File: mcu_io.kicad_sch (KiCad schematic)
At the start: 10 parts, among them U3 SiWG917Y, U9 PCAL6408AHK

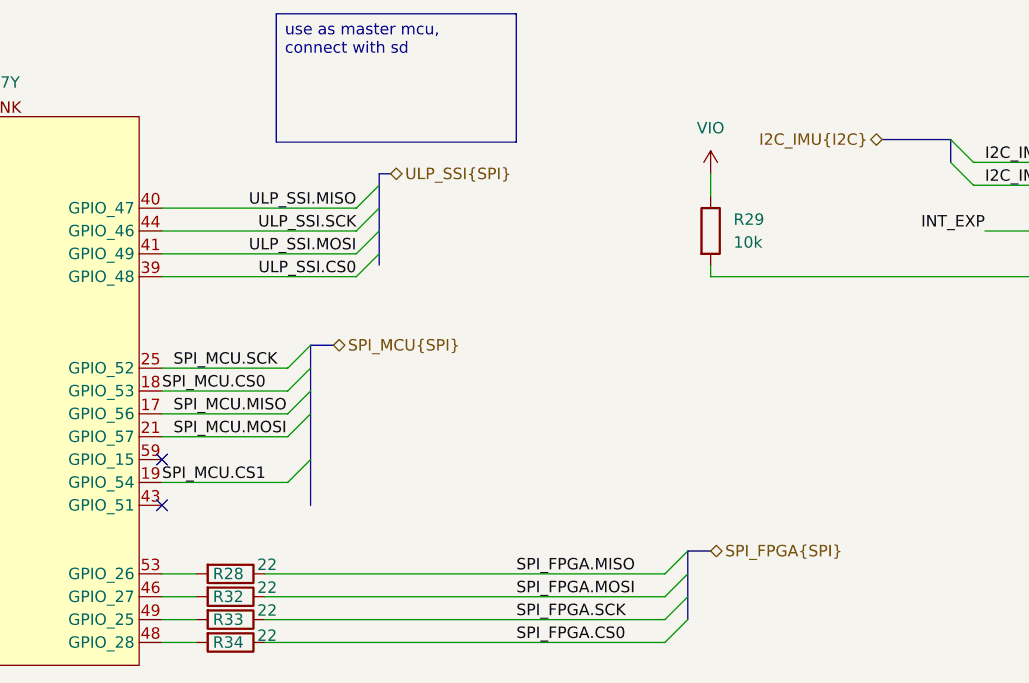
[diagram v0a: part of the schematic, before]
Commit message: new debug connector SOICbite, new board shape, new placement, addition of 22 ohm resistance in fast digital signals as spi
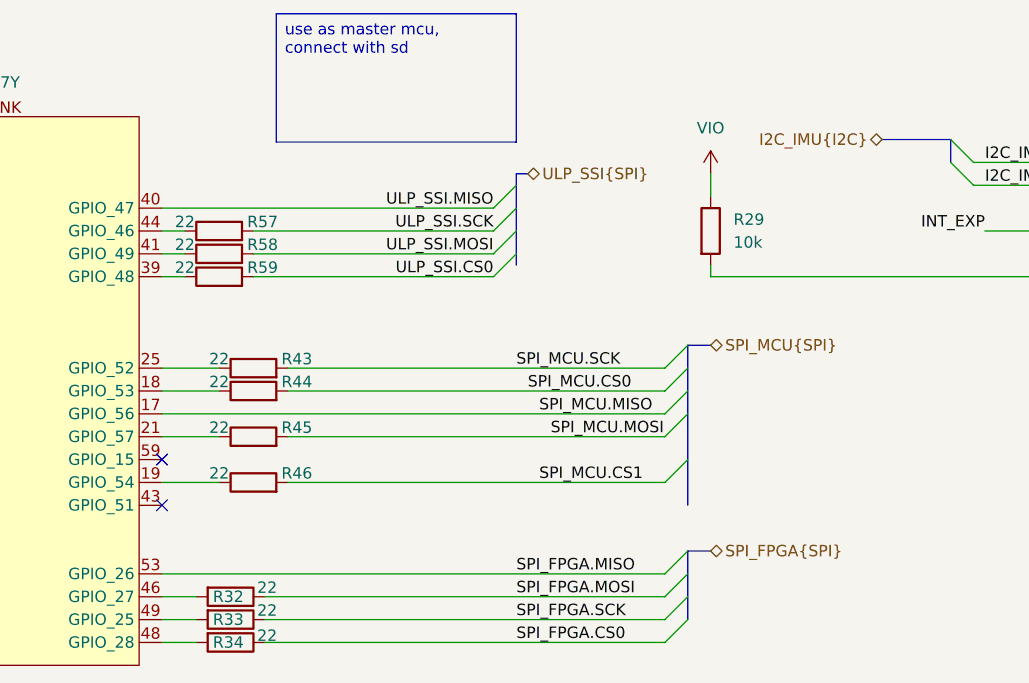
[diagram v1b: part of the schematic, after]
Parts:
- removed R28: 22, Resistor_SMD:R_0402_1005Metric, symbol #dzdb:g_res/R-22-0402
- added R43, R44, R45, R46, R57, R58, R59: 22, Resistor_SMD:R_0201_0603Metric, symbol #dzdb:g_res/R-22-0201
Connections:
- net SPI_FPGA.MISO: now also U3.53 (GPIO_26)
- net SPI_MCU.CS0: now also R44.2; no longer U3.18 (GPIO_53)
- net SPI_MCU.CS1: now also R46.2; no longer U3.19 (GPIO_54)
- net SPI_MCU.MOSI: now also R45.2; no longer U3.21 (GPIO_57)
- net SPI_MCU.SCK: now also R43.2; no longer U3.25 (GPIO_52)
- net ULP_SSI.CS0: now also R59.2; no longer U3.39 (GPIO_48)
- net ULP_SSI.MOSI: now also R58.2; no longer U3.41 (GPIO_49)
- net ULP_SSI.SCK: now also R57.2; no longer U3.44 (GPIO_46)
- new net: R43.1, U3.25 (GPIO_52)
- new net: R45.1, U3.21 (GPIO_57)
- new net: R46.1, U3.19 (GPIO_54)
- new net: R59.1, U3.39 (GPIO_48)
- new net: R44.1, U3.18 (GPIO_53)
- new net: R58.1, U3.41 (GPIO_49)
- new net: R57.1, U3.44 (GPIO_46)

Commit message: Comments on layout
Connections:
- net SPI_FPGA.CS0: now also R44.2; no longer R34.1
- net SPI_FPGA.MISO: now also U3.17 (GPIO_56); no longer U3.53 (GPIO_26)
- net SPI_FPGA.MOSI: now also R45.2; no longer R32.1
- net SPI_FPGA.SCK: now also R43.2; no longer R33.1
- net SPI_MCU.CS0: now also R34.1; no longer R44.2
- net SPI_MCU.MISO: now also U3.53 (GPIO_26); no longer U3.17 (GPIO_56)
- net SPI_MCU.MOSI: now also R32.1; no longer R45.2
- net SPI_MCU.SCK: now also R33.1; no longer R43.2
- net at R46.1: now also U3.47 (GPIO_29); no longer U3.19 (GPIO_54)
- no-connect marks 9 -> 8
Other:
- moved on the sheet: R46
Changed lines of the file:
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@@
-	)
-	(no_connect
-		(at 55.88 73.66)
 	)
 	(no_connect
@@
 	(wire
 		(pts
+			(xy 49.53 73.66) (xy 55.88 73.66)
+		)
+		(stroke
+			(width 0)
+			(type default)
+		)
+	)
+	(wire
+		(pts
 			(xy 96.52 71.12) (xy 99.06 71.12)
 		)
@@
 	(wire
 		(pts
-			(xy 110.49 99.06) (xy 152.4 99.06)
+			(xy 41.91 73.66) (xy 20.32 73.66)
 		)
 		(stroke
@@
 	)
 	(label "SPI_MCU.CS0"
-		(at 137.16 88.9 0)
+		(at 135.89 116.84 0)
 		(effects
 			(font
@@
 	)
 	(label "SPI_MCU.MOSI"
-		(at 139.7 93.98 0)
+		(at 135.89 111.76 0)
 		(effects
 			(font
@@
 	)
 	(label "SPI_FPGA.SCK"
-		(at 135.89 114.3 0)
+		(at 135.89 86.36 0)
 		(effects
 			(font
@@
 	)
 	(label "SPI_MCU.CS1"
-		(at 138.43 99.06 0)
-		(effects
-			(font
-				(size 1.27 1.27)
-			)
-			(justify left bottom)
+		(at 34.29 73.66 180)
+		(effects
+			(font
+				(size 1.27 1.27)
+			)
+			(justify right bottom)
 		)
 	)
@@
 	)
 	(label "SPI_FPGA.CS0"
-		(at 135.89 116.84 0)
+		(at 137.16 88.9 0)
 		(effects
 			(font
@@
 	)
 	(label "SPI_MCU.MISO"
-		(at 138.43 91.44 0)
+		(at 135.89 109.22 0)
 		(effects
 			(font
@@
 	)
 	(label "SPI_FPGA.MOSI"
-		(at 135.89 111.76 0)
+		(at 139.7 93.98 0)
 		(effects
 			(font
@@
 	)
 	(label "SPI_FPGA.MISO"
-		(at 135.89 109.22 0)
+		(at 138.43 91.44 0)
 		(effects
 			(font
@@
 	)
 	(label "SPI_MCU.SCK"
-		(at 135.89 86.36 0)
+		(at 135.89 114.3 0)
 		(effects
 			(font
@@
 	(hierarchical_label "SPI_MCU{SPI}"
 		(shape bidirectional)
-		(at 157.48 83.82 0)
+		(at 157.48 106.68 0)
 		(effects
 			(font
@@
 	(hierarchical_label "SPI_FPGA{SPI}"
 		(shape bidirectional)
-		(at 157.48 106.68 0)
+		(at 157.48 83.82 0)
 		(effects
 			(font
@@
 	(symbol
 		(lib_id "#dzdb:g_res/R-22-0201")
-		(at 106.68 99.06 90)
+		(at 45.72 73.66 270)
 		(unit 1)
 		(body_style 1)
@@
 		(dnp no)
 		(property "Reference" "R46"
-			(at 111.506 98.044 90)
+			(at 40.894 74.676 90)
 			(show_name no)
 			(do_not_autoplace no)
@@
 		)
 		(property "Value" "22"
-			(at 102.87 98.044 90)
+			(at 49.53 74.676 90)
 			(show_name no)
 			(do_not_autoplace no)
@@
 		)
 		(property "Footprint" "Resistor_SMD:R_0201_0603Metric"
-			(at 106.68 100.838 90)
+			(at 45.72 71.882 90)
 			(hide yes)
 			(show_name no)
@@
 		)
 		(property "Datasheet" "https://industrial.panasonic.com/ww/products/pt/general-purpose-chip-resistors/models/ERJ1GJF22R0C"
-			(at 106.68 99.06 0)
+			(at 45.72 73.66 0)
 			(hide yes)
 			(show_name no)
@@
 		)
 		(property "Description" "Res 22Ω 0201 0.05W Thick Film ±1%"
-			(at 106.68 99.06 0)
+			(at 45.72 73.66 0)
 			(hide yes)
 			(show_name no)
@@
 		)
 		(property "Power" "0.05W"
-			(at 106.68 99.06 0)
+			(at 45.72 73.66 0)
 			(hide yes)
 			(show_name no)
@@
 		)
 		(property "Tolerance" "1%"
-			(at 106.68 99.06 0)
+			(at 45.72 73.66 0)
 			(hide yes)
 			(show_name no)
@@
 		)
 		(property "Resistance" "22"
-			(at 106.68 99.06 0)
+			(at 45.72 73.66 0)
 			(hide yes)
 			(show_name no)
@@
 		)
 		(property "SPN" "667-ERJ-1GJF22R0C"
-			(at 106.68 99.06 0)
+			(at 45.72 73.66 0)
 			(hide yes)
 			(show_name no)
@@
 		)
 		(property "LCSC" "C20021234"
-			(at 106.68 99.06 0)
+			(at 45.72 73.66 0)
 			(hide yes)
 			(show_name no)
@@
 		)
 		(property "MPN" "ERJ-1GJF22R0C"
-			(at 106.68 99.06 0)
+			(at 45.72 73.66 0)
 			(hide yes)
 			(show_name no)
@@
 		)
 		(property "Supplier" "Mouser"
-			(at 106.68 99.06 0)
+			(at 45.72 73.66 0)
 			(hide yes)
 			(show_name no)
@@
 		)
 		(property "Manufacturer" "Panasonic"
-			(at 106.68 99.06 0)
+			(at 45.72 73.66 0)
 			(hide yes)
 			(show_name no)
@@
 		)
 		(property "IPN" "R-22-0201"
-			(at 106.68 99.06 0)
+			(at 45.72 73.66 0)
 			(hide yes)
 			(show_name no)
@@
 		)
 		(property "Material" "Thick Film"
-			(at 106.68 99.06 0)
+			(at 45.72 73.66 0)
 			(hide yes)
 			(show_name no)
@@
 		)
 		(property "Comment" "lifecycle=Active;note=AEC-Q200 compliant;TCR=±200ppm/°C"
-			(at 106.68 99.06 0)
-			(hide yes)
-			(show_name no)
+			(at 45.72 73.66 0)
+			(hide yes)
+			(show_name no)

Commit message: updated routing SPI, change 0402 to 0201
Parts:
- removed C44, C48: 100nF, Capacitor_SMD:C_0402_1005Metric, symbol #dzdb:g_cap/C-100n-0402
- added C42, C43: 100nF, Capacitor_SMD:C_0201_0603Metric, symbol #dzdb:g_cap/C-100n-0201
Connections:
- net GND: now also C42.2, C43.2
- net VIO: now also C42.1, C43.1
- no-connect marks 8 -> 9

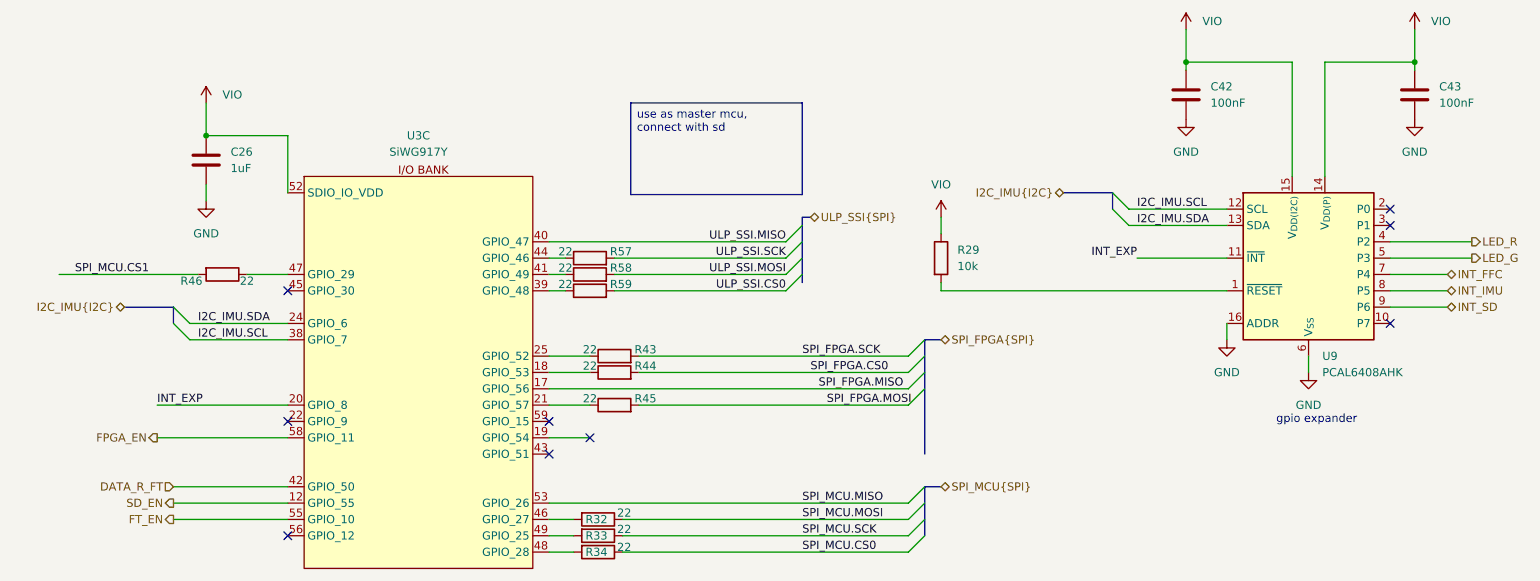
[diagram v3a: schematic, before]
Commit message: Add comments from layout meeting 20.07.2026
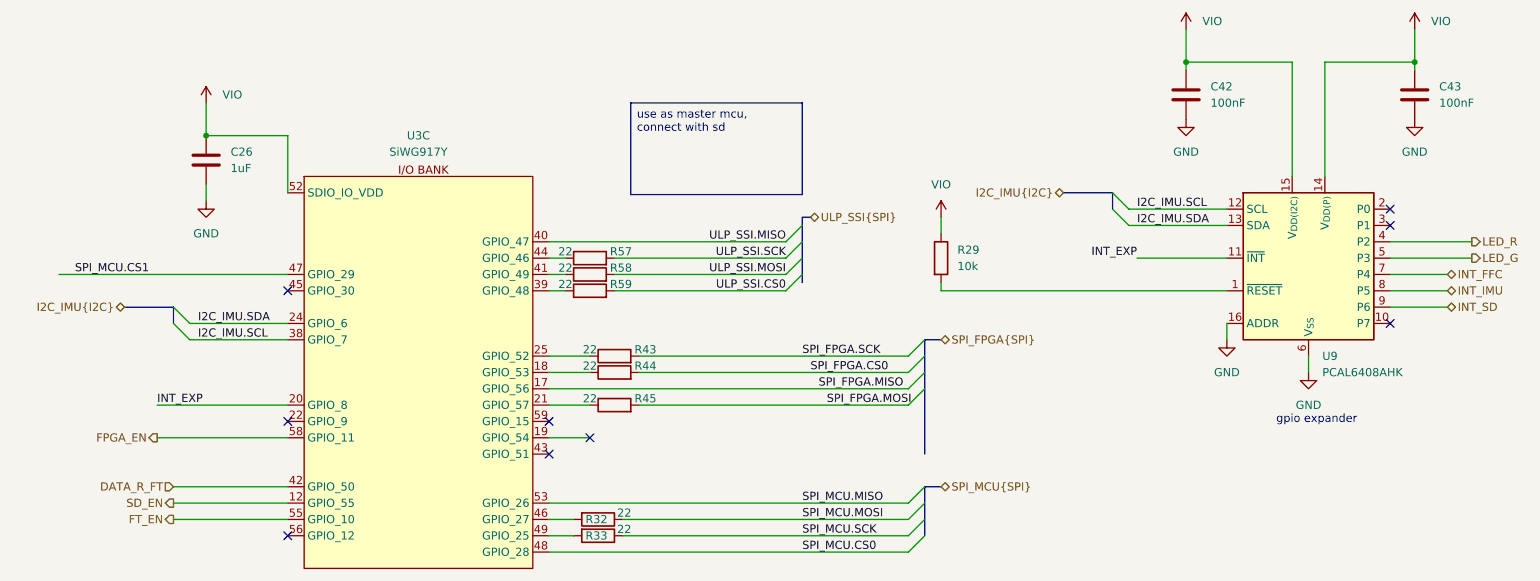
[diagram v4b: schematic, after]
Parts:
- removed R34: 22, Resistor_SMD:R_0402_1005Metric, symbol #dzdb:g_res/R-22-0402
- removed R46: 22, Resistor_SMD:R_0201_0603Metric, symbol #dzdb:g_res/R-22-0201
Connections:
- net SPI_MCU.CS0: now also U3.48 (GPIO_28)
- net SPI_MCU.CS1: now also U3.47 (GPIO_29)
